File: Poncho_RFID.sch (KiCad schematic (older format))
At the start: 2 parts

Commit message: Actualizado eeschema
Circuito alrededor del integrado completo
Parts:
- added C? (x2): 10nF, symbol C
- added C? (x2): 100nF, symbol C
- added C? (x2): 1uF, symbol CP1
- added FL?: 744232222, symbol EMI_Filter_CommonMode
- added L? (x2): 742792042, symbol L_Core_Ferrite
- added L?: 742792093, symbol L
- added R? (x2): 0, symbol R
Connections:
- new net: FL?.2, L?.1
- new net: FL?.4, L?.1
- new net: L?.2, R?.1 (x2)
- new net: C?.1, C?.1, C?.1, L?.2, R?.2
- new net: C?.1, C?.1, C?.1, L?.1
- new net +3V3: FL?.1, FL?.3
- new net GND: C?.2, C?.2, C?.2, C?.2, C?.2, C?.2, R?.2
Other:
- moved on the sheet: XA?A, XA?B

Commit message: Prueba despues del error de MEGAsync
Este commit hay que hacerle un rebase
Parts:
- gave numbers to parts that had none: 13
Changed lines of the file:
@@
 $EndSheet
 $Comp
-L Conn_Poncho2P_2x_20x2 XA?
+L Conn_Poncho2P_2x_20x2 XA1
 U 1 1 59C6DCF5
 P 8950 3850
-F 0 "XA?" H 9250 4250 60  0000 C CNN
+F 0 "XA1" H 9250 4250 60  0000 C CNN
 F 1 "Conn_Poncho2P_2x_20x2" H 9300 2150 60  0000 C CNN
 F 2 "" H 8950 3850 60  0000 C CNN
@@
 $EndComp
 $Comp
-L Conn_Poncho2P_2x_20x2 XA?
+L Conn_Poncho2P_2x_20x2 XA1
 U 2 1 59C6DD3A
 P 7300 3850
-F 0 "XA?" H 7600 4250 60  0000 C CNN
+F 0 "XA1" H 7600 4250 60  0000 C CNN
 F 1 "Conn_Poncho2P_2x_20x2" H 7650 2150 60  0000 C CNN
 F 2 "" H 7300 3850 60  0000 C CNN
@@
 $EndComp
 $Comp
-L +3.3V #PWR?
+L +3.3V #PWR3
 U 1 1 59D0AE5B
 P 1700 850
-F 0 "#PWR?" H 1700 700 50  0001 C CNN
+F 0 "#PWR3" H 1700 700 50  0001 C CNN
 F 1 "+3.3V" H 1700 990 50  0000 C CNN
 F 2 "" H 1700 850 50  0001 C CNN
@@
 $EndComp
 $Comp
-L EMI_Filter_CommonMode FL?
+L EMI_Filter_CommonMode FL1
 U 1 1 59D0AE79
 P 1700 1350
-F 0 "FL?" H 1700 1525 50  0000 C CNN
+F 0 "FL1" H 1700 1525 50  0000 C CNN
 F 1 "744232222" H 1700 1600 50  0000 C CNN
 F 2 "" V 1700 1390 50  0000 C CNN
@@
 Connection ~ 1700 900
 $Comp
-L L_Core_Ferrite L?
+L L_Core_Ferrite L2
 U 1 1 59D0B56F
 P 1800 1950
-F 0 "L?" V 1750 1950 50  0000 C CNN
+F 0 "L2" V 1750 1950 50  0000 C CNN
 F 1 "742792042" V 1650 1950 50  0000 C CNN
 F 2 "" H 1800 1950 50  0001 C CNN
@@
 $EndComp
 $Comp
-L L_Core_Ferrite L?
+L L_Core_Ferrite L1
 U 1 1 59D0B576
 P 1600 1950
-F 0 "L?" V 1550 1950 50  0000 C CNN
+F 0 "L1" V 1550 1950 50  0000 C CNN
 F 1 "742792042" V 1710 1950 50  0000 C CNN
 F 2 "" H 1600 1950 50  0001 C CNN
@@
 	1600 1550 1600 1800
 $Comp
-L R R?
+L R R1
 U 1 1 59D0B71E
 P 1600 2400
-F 0 "R?" V 1680 2400 50  0000 C CNN
+F 0 "R1" V 1680 2400 50  0000 C CNN
 F 1 "0" V 1600 2400 50  0000 C CNN
 F 2 "" V 1530 2400 50  0001 C CNN
@@
 $EndComp
 $Comp
-L R R?
+L R R2
 U 1 1 59D0B766
 P 1800 2400
-F 0 "R?" V 1880 2400 50  0000 C CNN
+F 0 "R2" V 1880 2400 50  0000 C CNN
 F 1 "0" V 1800 2400 50  0000 C CNN
 F 2 "" V 1730 2400 50  0001 C CNN
@@
 	1800 2250 1800 2100
 $Comp
-L GND #PWR?
+L GND #PWR4
 U 1 1 59D0B834
 P 1800 2650
-F 0 "#PWR?" H 1800 2400 50  0001 C CNN
+F 0 "#PWR4" H 1800 2400 50  0001 C CNN
 F 1 "GND" H 1800 2500 50  0000 C CNN
 F 2 "" H 1800 2650 50  0001 C CNN
@@
 	1800 2650 1800 2550
 $Comp
-L VPS_MAIN #PWR?
+L VPS_MAIN #PWR1
 U 1 1 59D0B937
 P 1200 3000
-F 0 "#PWR?" H 1400 3050 60  0001 C CNN
+F 0 "#PWR1" H 1400 3050 60  0001 C CNN
 F 1 "VPS_MAIN" H 1200 3150 60  0000 C CNN
 F 2 "" H 1200 3000 60  0001 C CNN
@@
 $EndComp
 $Comp
-L VPS_TX #PWR?
+L VPS_TX #PWR5
 U 1 1 59D0B959
 P 2750 3000
-F 0 "#PWR?" H 2950 3050 60  0001 C CNN
+F 0 "#PWR5" H 2950 3050 60  0001 C CNN
 F 1 "VPS_TX" H 2750 3150 60  0000 C CNN
 F 2 "" H 2750 3000 60  0001 C CNN
@@
 $EndComp
 $Comp
-L L L?
+L L L3
 U 1 1 59D0BAE0
 P 2000 3100
-F 0 "L?" V 1950 3100 50  0000 C CNN
+F 0 "L3" V 1950 3100 50  0000 C CNN
 F 1 "742792093" V 2075 3100 50  0000 C CNN
 F 2 "" H 2000 3100 50  0001 C CNN
@@
 $EndComp
 $Comp
-L C C?
+L C C1
 U 1 1 59D0BB15
 P 850 3300
-F 0 "C?" H 875 3400 50  0000 L CNN
+F 0 "C1" H 875 3400 50  0000 L CNN
 F 1 "10nF" H 875 3200 50  0000 L CNN
 F 2 "" H 888 3150 50  0001 C CNN
@@
 $EndComp
 $Comp
-L C C?
+L C C2
 U 1 1 59D0BB43
 P 1200 3300
-F 0 "C?" H 1225 3400 50  0000 L CNN
+F 0 "C2" H 1225 3400 50  0000 L CNN
 F 1 "100nF" H 1225 3200 50  0000 L CNN
 F 2 "" H 1238 3150 50  0001 C CNN
@@
 $EndComp
 $Comp
-L CP1 C?
+L CP1 C3
 U 1 1 59D0BB73
 P 1600 3300
-F 0 "C?" H 1625 3400 50  0000 L CNN
+F 0 "C3" H 1625 3400 50  0000 L CNN
 F 1 "1uF" H 1625 3200 50  0000 L CNN
 F 2 "" H 1600 3300 50  0001 C CNN
@@
 Connection ~ 1200 3500
 $Comp
-L GND #PWR?
+L GND #PWR2
 U 1 1 59D0BED1
 P 1200 3600
-F 0 "#PWR?" H 1200 3350 50  0001 C CNN
+F 0 "#PWR2" H 1200 3350 50  0001 C CNN
 F 1 "GND" H 1200 3450 50  0000 C CNN
 F 2 "" H 1200 3600 50  0001 C CNN
@@
 $EndComp
 $Comp
-L C C?
+L C C4
 U 1 1 59D0BFED
 P 2400 3300
-F 0 "C?" H 2425 3400 50  0000 L CNN
+F 0 "C4" H 2425 3400 50  0000 L CNN
 F 1 "10nF" H 2425 3200 50  0000 L CNN
 F 2 "" H 2438 3150 50  0001 C CNN
@@
 $EndComp
 $Comp
-L C C?
+L C C5
 U 1 1 59D0BFF3
 P 2750 3300
-F 0 "C?" H 2775 3400 50  0000 L CNN
+F 0 "C5" H 2775 3400 50  0000 L CNN
 F 1 "100nF" H 2775 3200 50  0000 L CNN
 F 2 "" H 2788 3150 50  0001 C CNN
@@
 $EndComp
 $Comp
-L CP1 C?
+L CP1 C6
 U 1 1 59D0BFF9
 P 3150 3300
-F 0 "C?" H 3175 3400 50  0000 L CNN
+F 0 "C6" H 3175 3400 50  0000 L CNN
 F 1 "1uF" H 3175 3200 50  0000 L CNN
 F 2 "" H 3150 3300 50  0001 C CNN
@@
 Connection ~ 2750 3500
 $Comp
-L GND #PWR?
+L GND #PWR6
 U 1 1 59D0C004
 P 2750 3600
-F 0 "#PWR?" H 2750 3350 50  0001 C CNN
+F 0 "#PWR6" H 2750 3350 50  0001 C CNN
 F 1 "GND" H 2750 3450 50  0000 C CNN
 F 2 "" H 2750 3600 50  0001 C CNN

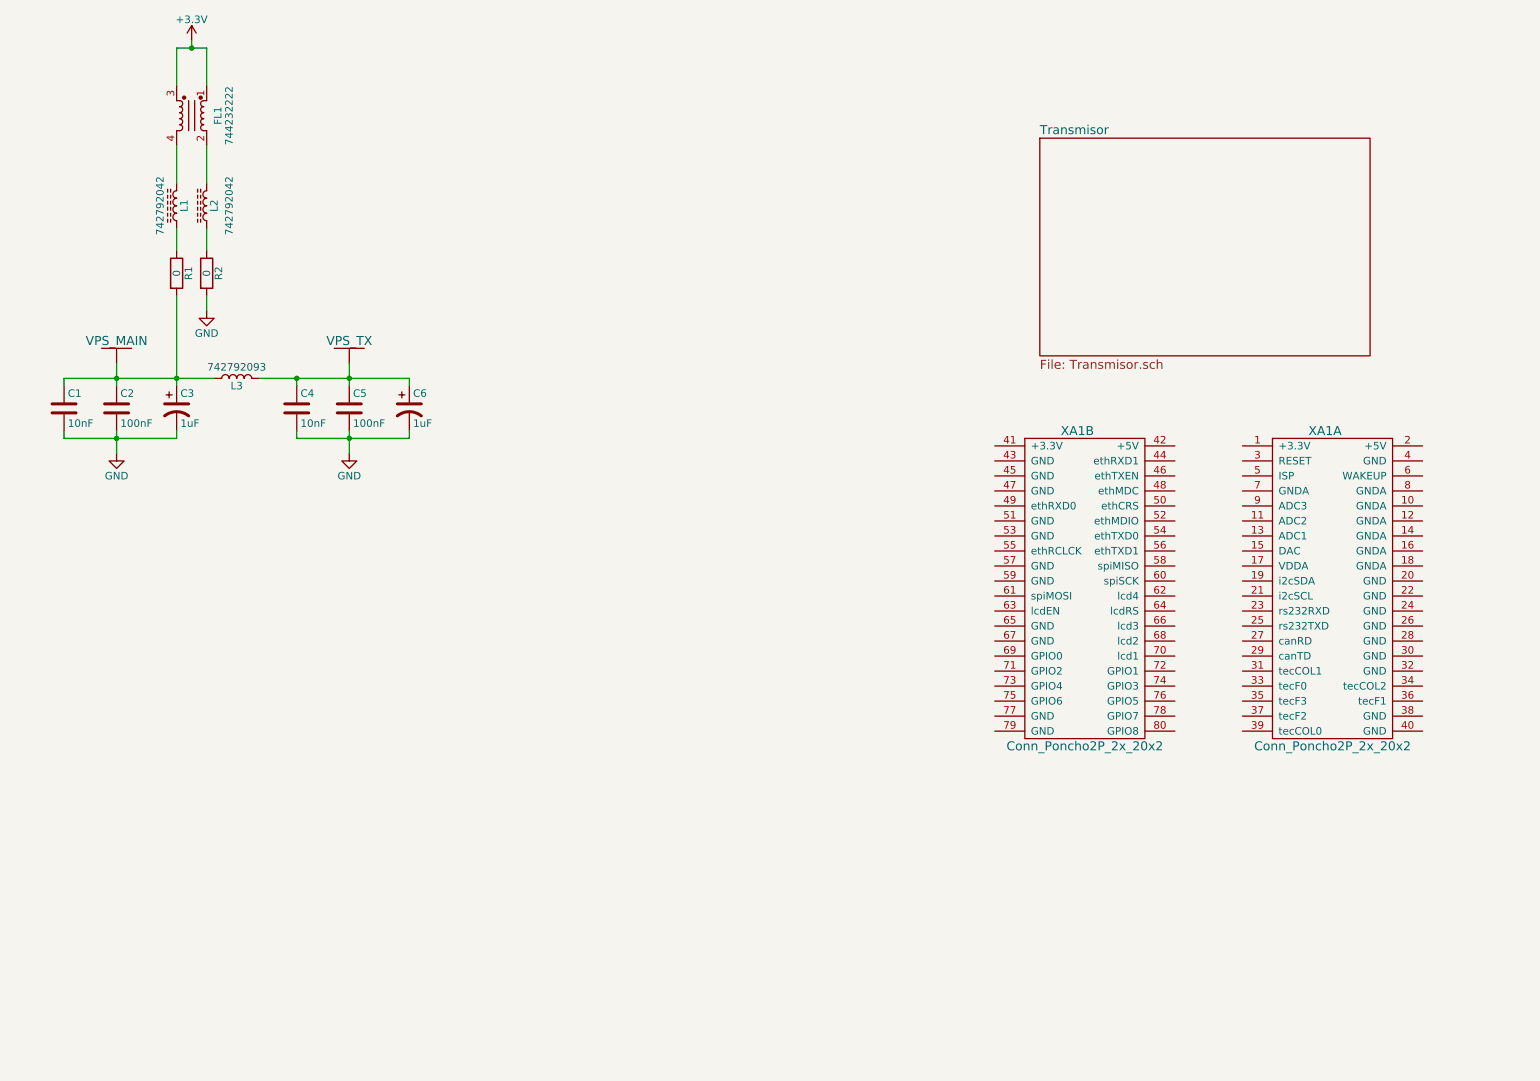
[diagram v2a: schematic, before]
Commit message: Reestructuracion de esquematico
Entra todo en una sola pagina, por lo que no hice separacion jerarquica. Actualizados footprints y algunos campos para Kicost
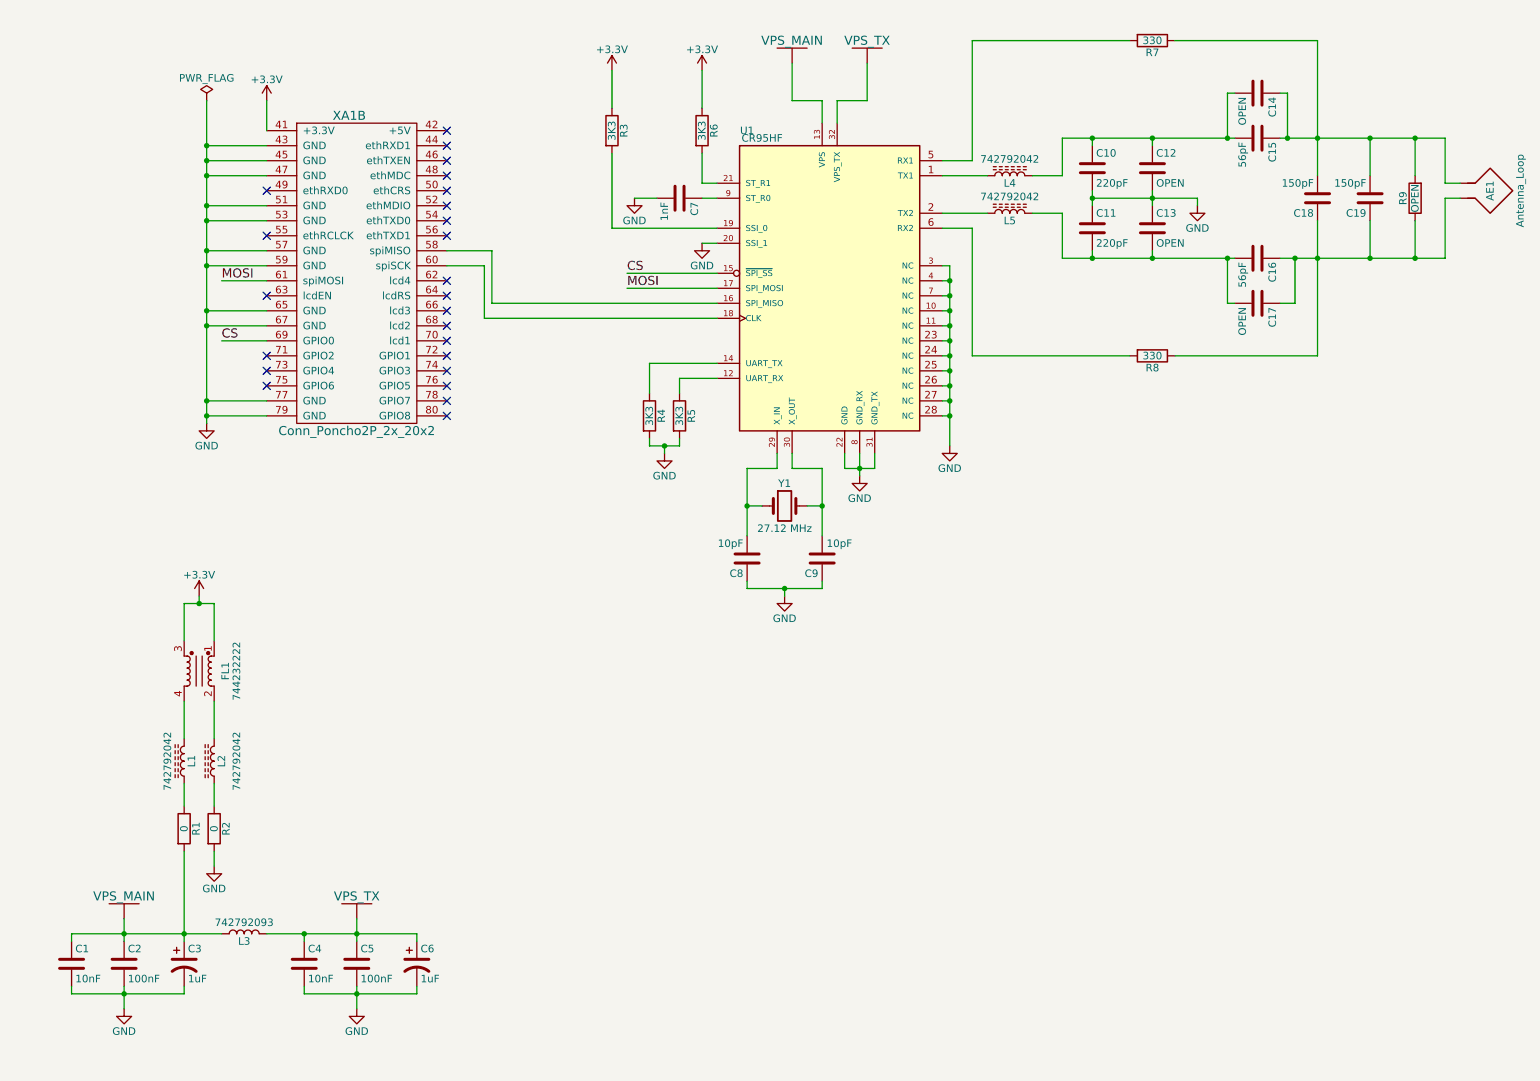
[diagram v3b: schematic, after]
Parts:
- removed unit 1 of XA1
- added AE1: Antenna_Loop, symbol Antenna_Loop
- added C10, C11: 220pF, Capacitors_SMD:C_0805_HandSoldering, symbol C
- added C12, C13, C14, C17: OPEN, Capacitors_SMD:C_0805_HandSoldering, symbol C
- added C15, C16: 56pF, Capacitors_SMD:C_0805_HandSoldering, symbol C
- added C18, C19: 150pF, Capacitors_SMD:C_0805_HandSoldering, symbol C
- added C7: 1nF, Capacitors_SMD:C_0805_HandSoldering, symbol C
- added C8, C9: 10pF, Capacitors_SMD:C_0805_HandSoldering, symbol C
- added L4, L5: 742792042, Inductors_SMD:L_0805_HandSoldering, symbol L_Core_Ferrite
- added R3, R4, R5, R6: 3K3, Resistors_SMD:R_0805_HandSoldering, symbol R
- added R7, R8: 330, Resistors_SMD:R_0805_HandSoldering, symbol R
- added R9: OPEN, Resistors_SMD:R_0805_HandSoldering, symbol R
- added U1: CR95HF, Housings_DFN_QFN:QFN-32-1EP_5x5mm_Pitch0.5mm, symbol CR95HF
- added Y1: 27.12 MHz, Crystals:Crystal_SMD_5032-2pin_5.0x3.2mm, symbol Crystal
- C1, C2, C3, C4, C5, C6: footprint (none) -> Capacitors_SMD:C_0805_HandSoldering
- FL1: footprint (none) -> Inductors_SMD:L_CommonMode_Wuerth_WE-SL2; Digikey# (none) -> 732-1474-1-ND; Manf (none) -> Wurth Electronics Inc.; Manf# (none) -> 744232222
- L1, L2: footprint (none) -> Inductors_SMD:L_0805_HandSoldering; Digikey# (none) -> 732-4642-1-ND; Manf (none) -> Wurth Electronics Inc.; Manf# (none) -> 742792042
- L3: footprint (none) -> Inductors_SMD:L_0805_HandSoldering
- R1, R2: footprint (none) -> Resistors_SMD:R_0805_HandSoldering
- XA1: footprint (none) -> Pin_Headers:Pin_Header_Straight_2x20_Pitch1.00mm
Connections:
- net +3V3: now also XA1.41 (+3.3V), R3.1, R6.1
- net GND: now also XA1.43 (GND), XA1.45 (GND), XA1.47 (GND), XA1.51 (GND), XA1.53 (GND), XA1.57 (GND), XA1.59 (GND), XA1.65 (GND), XA1.67 (GND), XA1.77 (GND), XA1.79 (GND), C10.2, C11.1, C12.2, C13.1, C7.2, C8.1, C9.1, R4.2, R5.2, U1.10 (NC), U1.11 (NC), U1.20 (SSI_1), U1.22 (GND), U1.23 (NC), U1.24 (NC), U1.25 (NC), U1.26 (NC), U1.27 (NC), U1.28 (NC), U1.3 (NC), U1.31 (GND_TX), U1.4 (NC), U1.7 (NC), U1.8 (GND_RX)
- net at XA1.58 (spiMISO): now also U1.16 (SPI_MISO)
- net at XA1.60 (spiSCK): now also U1.18 (CLK)
- net MOSI: now reaches XA1.61 (spiMOSI)
- net MOSI: now also U1.17 (SPI_MOSI)
- net CS: now reaches XA1.69 (GPIO0)
- net CS: now also U1.15 (~SPI_SS)
- new net: R3.2, U1.19 (SSI_0)
- new net: C7.1, U1.9 (ST_R0)
- new net: R6.2, U1.21 (ST_R1)
- new net: C8.2, U1.29 (X_IN), Y1.1
- new net: C9.2, U1.30 (X_OUT), Y1.2
- new net: R5.1, U1.12 (UART_RX)
- new net: R4.1, U1.14 (UART_TX)
- new net: C11.2, C13.2, C16.2, C17.2, L5.1
- new net: L5.2, U1.2 (TX2)
- new net: C10.1, C12.1, C14.2, C15.2, L4.1
- new net: L4.2, U1.1 (TX1)
- new net: R7.2, U1.5 (RX1)
- new net: R8.2, U1.6 (RX2)
- new net: AE1.1, C14.1, C15.1, C18.2, C19.2, R7.1, R9.2
- new net: AE1.2, C16.1, C17.1, C18.1, C19.1, R8.1, R9.1
- no-connect marks 0 -> 24
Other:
- moved on the sheet: C1, C2, C3, C4, C5, C6, FL1, L1, L2, L3, R1, R2

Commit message: Actualizacion esquematico
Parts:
- added unit 1 of XA1
- XA1: footprint Pin_Headers:Pin_Header_Straight_2x20_Pitch1.00mm -> poncho_RFID:Conn_Poncho_Chico
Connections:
- net +3V3: now also XA1.1 (+3.3V)
- net GND: now also XA1.10 (GNDA), XA1.12 (GNDA), XA1.14 (GNDA), XA1.16 (GNDA), XA1.18 (GNDA), XA1.20 (GND), XA1.22 (GND), XA1.24 (GND), XA1.26 (GND), XA1.28 (GND), XA1.30 (GND), XA1.32 (GND), XA1.38 (GND), XA1.4 (GND), XA1.40 (GND), XA1.8 (GNDA)
- no-connect marks 24 -> 47
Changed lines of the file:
@@
 F 0 "XA1" H 2750 2150 60  0000 C CNN
 F 1 "Conn_Poncho2P_2x_20x2" H 2800 50  60  0000 C CNN
-F 2 "Pin_Headers:Pin_Header_Straight_2x20_Pitch1.00mm" H 2450 1750 60  0001 C CNN
+F 2 "poncho_RFID:Conn_Poncho_Chico" H 2450 1750 60  0001 C CNN
 F 3 "" H 2450 1750 60  0000 C CNN
 	2    2450 1750
@@
 Wire Wire Line
 	2200 1250 2200 1450
+$Comp
+L GND #PWR021
+U 1 1 59E17C94
+P 4950 7500
+F 0 "#PWR021" H 4950 7250 50  0001 C CNN
+F 1 "GND" H 4950 7350 50  0000 C CNN
+F 2 "" H 4950 7500 50  0001 C CNN
+F 3 "" H 4950 7500 50  0001 C CNN
+	1    4950 7500
+	1    0    0    -1
+$EndComp
+Wire Wire Line
+	5100 7250 4950 7250
+Wire Wire Line
+	4950 5550 4950 7500
+Wire Wire Line
+	5100 7350 4950 7350
+Connection ~ 4950 7350
+Wire Wire Line
+	5100 6250 4950 6250
+Connection ~ 4950 7250
+Wire Wire Line
+	5100 6650 4950 6650
+Connection ~ 4950 6650
+Wire Wire Line
+	5100 6750 4950 6750
+Connection ~ 4950 6750
+Wire Wire Line
+	5100 6350 4950 6350
+Connection ~ 4950 6350
+Wire Wire Line
+	5100 6050 4950 6050
+Connection ~ 4950 6250
+Wire Wire Line
+	5100 5950 4950 5950
+Connection ~ 4950 6050
+Connection ~ 4950 5950
+Wire Wire Line
+	5100 5750 4950 5750
+Connection ~ 4950 5750
+Wire Wire Line
+	5100 5550 4950 5550
+NoConn ~ 6300 5550
+NoConn ~ 6300 5650
+NoConn ~ 6300 5750
+NoConn ~ 6300 5850
+NoConn ~ 6300 5950
+NoConn ~ 6300 6050
+NoConn ~ 6300 6150
+NoConn ~ 6300 6250
+NoConn ~ 6300 6350
+NoConn ~ 6300 6450
+NoConn ~ 6300 6550
+NoConn ~ 6300 6650
+NoConn ~ 6300 6750
+NoConn ~ 6300 6850
+NoConn ~ 6300 6950
+NoConn ~ 6300 7050
+NoConn ~ 6300 7150
+NoConn ~ 6300 7250
+NoConn ~ 6300 7350
+NoConn ~ 5100 7150
+NoConn ~ 5100 7050
+Wire Wire Line
+	5100 6450 4950 6450
+Connection ~ 4950 6450
+Wire Wire Line
+	5100 6550 4950 6550
+Connection ~ 4950 6550
+$Comp
+L Conn_Poncho2P_2x_20x2 XA1
+U 1 1 59E16F73
+P 6050 5750
+F 0 "XA1" H 6350 6150 60  0000 C CNN
+F 1 "Conn_Poncho2P_2x_20x2" H 6400 4050 60  0000 C CNN
+F 2 "poncho_RFID:Conn_Poncho_Chico" H 6050 5750 60  0001 C CNN
+F 3 "" H 6050 5750 60  0000 C CNN
+	1    6050 5750
+	-1   0    0    -1
+$EndComp
+Wire Wire Line
+	5100 6850 4950 6850
+Connection ~ 4950 6850
+Wire Wire Line
+	4950 6950 5100 6950
+Connection ~ 4950 6950
+NoConn ~ 5100 5450
+NoConn ~ 5100 5650
+Wire Wire Line
+	5100 5850 4950 5850
+Connection ~ 4950 5850
+Wire Wire Line
+	5100 6150 4950 6150
+Connection ~ 4950 6150
+$Comp
+L +3.3V #PWR022
+U 1 1 59E1B372
+P 6450 5400
+F 0 "#PWR022" H 6450 5250 50  0001 C CNN
+F 1 "+3.3V" H 6450 5540 50  0000 C CNN
+F 2 "" H 6450 5400 50  0001 C CNN
+F 3 "" H 6450 5400 50  0001 C CNN
+	1    6450 5400
+	1    0    0    -1
+$EndComp
+Wire Wire Line
+	6450 5400 6450 5450
+Wire Wire Line
+	6450 5450 6300 5450
 $EndSCHEMATC

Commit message: completado campos kicost
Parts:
- removed C3, C6: 1uF, Capacitors_SMD:C_0805_HandSoldering, symbol CP1
- added C3, C6: 1uF, symbol C
- C1, C4: Digikey# (none) -> 311-1136-1-ND; Manf (none) -> Yageo; Manf# (none) -> CC0805KRX7R9BB103
- C10, C11: Digikey# (none) -> 712-1398-1-ND; Manf (none) -> Johanson Technology Inc.; Manf# (none) -> 251R15S221JV4E
- C15, C16: Digikey# (none) -> 1276-1833-1-ND; Manf (none) -> Samsung Electro-Mechanics; Manf# (none) -> CL21C560JBANNNC
- C18, C19: Digikey# (none) -> 399-1125-1-ND; Manf (none) -> KEMET; Manf# (none) -> C0805C151J5GACTU
- C2, C5: Digikey# (none) -> 478-1395-1-ND; Manf (none) -> AVX Corporation; Manf# (none) -> 08055C104KAT2A
- C7: Digikey# (none) -> 399-1147-1-ND; Manf (none) -> KEMET; Manf# (none) -> C0805C102K5RACTU
- C8, C9: Digikey# (none) -> 399-7062-1-ND; Manf (none) -> KEMET; Manf# (none) -> C0805C100JDGACTU
- R1, R2: footprint Resistors_SMD:R_0805_HandSoldering -> Resistors_SMD:R_1206_HandSoldering; Digikey# (none) -> RCL0.0CCT-ND; Manf (none) -> Vishay Dale; Manf# (none) -> RCL06120000Z0EA
- R3, R4, R5, R6: Digikey# (none) -> RHM3.3KBUCT-ND; Manf (none) -> Rohm Semiconductor; Manf# (none) -> LTR10EZPJ332
- R7, R8: Digikey# (none) -> RHM1215CT-ND; Manf (none) -> Rohm Semiconductor; Manf# (none) -> LTR10EZPF3300
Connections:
- net +3V3: no longer R3.1, R6.1, XA1.41 (+3.3V)
- net GND: now also C3.2, C6.2
- net VPS_MAIN: now reaches C1.1, C2.1, L3.2, R1.2
- net VPS_MAIN: now also R3.1, R6.1, U1.13 (VPS), C3.1
- net VPS_TX: now reaches C4.1, C5.1, L3.1
- net VPS_TX: now also U1.32 (VPS_TX), C6.1
- no-connect marks 47 -> 48

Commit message: PCB definido
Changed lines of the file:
@@
 	1    0    0    -1
 $EndComp
-Text GLabel 2950 6400 2    60   Input ~ 0
-VPS_TX
-Text GLabel 6050 900  2    60   Input ~ 0
-VPS_TX
 $Comp
 L PWR_FLAG #FLG019
@@
 	1    0    0    -1
 $EndComp
-Text GLabel 1150 6400 0    60   Input ~ 0
-VPS_MAIN
 Wire Wire Line
 	1650 4850 1650 4600
@@
 Wire Wire Line
 	5850 900  5900 900
-Text GLabel 5850 900  0    60   Input ~ 0
-VPS_MAIN
 $Comp
 L C C3
@@
 Wire Wire Line
 	6000 900  6050 900
-Text GLabel 4450 1050 0    60   Input ~ 0
-VPS_MAIN
 Wire Wire Line
 	4450 1050 5100 1050
@@
 	4500 1300 4500 1050
 Connection ~ 4500 1050
+Text Label 1150 6400 2    60   ~ 0
+VPS_MAIN
+Text Label 4450 1050 2    60   ~ 0
+VPS_MAIN
+Text Label 5850 900  2    60   ~ 0
+VPS_MAIN
+Text Label 6050 900  0    60   ~ 0
+VPS_TX
+Text Label 2950 6400 0    60   ~ 0
+VPS_TX
 $EndSCHEMATC
